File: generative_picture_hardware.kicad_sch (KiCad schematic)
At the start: 59 parts, among them J1 e_Paper_HAT, J2 Conn_ARM_JTAG_SWD_10, J3 USB_C_Receptacle_USB2.0, Q1 PMN48XP, Q2 DMG9926UDM, Q3 MBT3904DW1, SW1 SW_Push, SW2 SW_Push, U1 AP2112K-3.3, U2 ESP32-WROOM-32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

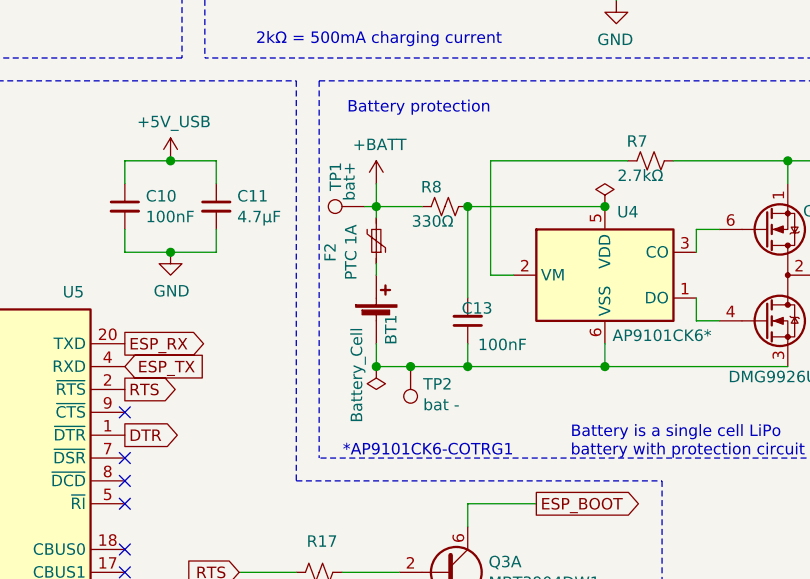
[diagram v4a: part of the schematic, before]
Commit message: Removes battery test points and adds labels to JTAG connector
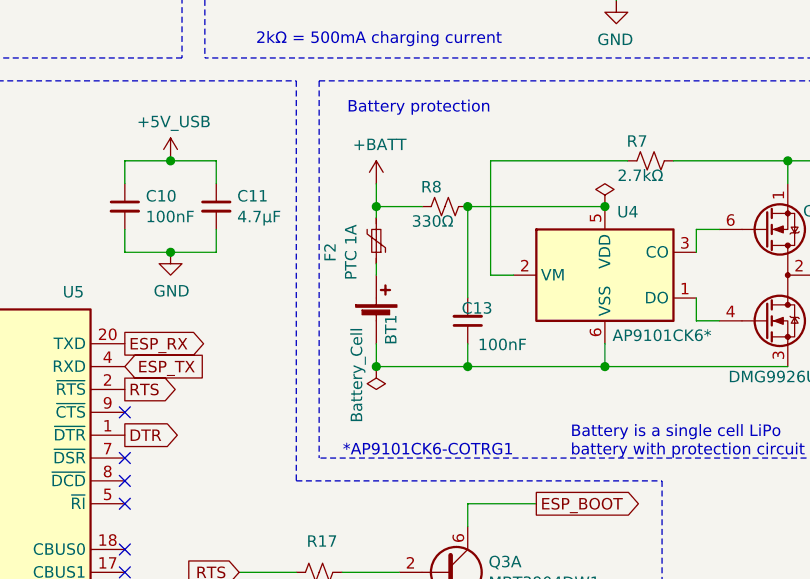
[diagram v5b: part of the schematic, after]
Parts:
- removed TP1: bat+, TestPoint:TestPoint_Pad_D2.0mm, symbol Connector:TestPoint
- removed TP2: bat -, TestPoint:TestPoint_Pad_D2.0mm, symbol Connector:TestPoint
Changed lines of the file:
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@@
   (junction (at 143.51 143.51) (diameter 1.016) (color 0 0 0 0))
   (junction (at 146.05 39.37) (diameter 1.016) (color 0 0 0 0))
-  (junction (at 147.32 143.51) (diameter 1.016) (color 0 0 0 0))
   (junction (at 153.67 125.73) (diameter 1.016) (color 0 0 0 0))
   (junction (at 153.67 143.51) (diameter 1.016) (color 0 0 0 0))
@@
     (stroke (width 0) (type solid) (color 0 0 0 0))
   )
-  (wire (pts (xy 142.24 125.73) (xy 143.51 125.73))
-    (stroke (width 0) (type solid) (color 0 0 0 0))
-  )
   (wire (pts (xy 143.51 39.37) (xy 146.05 39.37))
     (stroke (width 0) (type solid) (color 0 0 0 0))
@@
     (stroke (width 0) (type solid) (color 0 0 0 0))
   )
-  (wire (pts (xy 143.51 143.51) (xy 147.32 143.51))
+  (wire (pts (xy 143.51 143.51) (xy 153.67 143.51))
     (stroke (width 0) (type solid) (color 0 0 0 0))
   )
@@
     (stroke (width 0) (type solid) (color 0 0 0 0))
   )
-  (wire (pts (xy 147.32 143.51) (xy 153.67 143.51))
-    (stroke (width 0) (type solid) (color 0 0 0 0))
-  )
   (wire (pts (xy 153.67 125.73) (xy 153.67 135.89))
     (stroke (width 0) (type solid) (color 0 0 0 0))
@@
     (pin "1")
   )
-  (symbol (lib_id "Connector:TestPoint") (at 142.24 125.73 90) (unit 1)
-    (in_bom yes) (on_board yes)
-    (property "Reference" "TP1" (id 0) (at 139.0079 120.7771 0)
-      (effects (font (size 1.27 1.27)) (justify right))
-    )
-    (property "Value" "bat+" (id 1) (at 140.519 120.777 0)
-      (effects (font (size 1.27 1.27)) (justify right))
-    )
-    (property "Footprint" "TestPoint:TestPoint_Pad_D2.0mm" (id 2) (at 142.24 120.65 0)
-      (effects (font (size 1.27 1.27)) hide)
-    )
-    (property "Datasheet" "~" (id 3) (at 142.24 120.65 0)
-      (effects (font (size 1.27 1.27)) hide)
-    )
-    (pin "1")
-  )
-  (symbol (lib_id "Connector:TestPoint") (at 147.32 143.51 180) (unit 1)
-    (in_bom yes) (on_board yes)
-    (property "Reference" "TP2" (id 0) (at 148.7171 145.4721 0)
-      (effects (font (size 1.27 1.27)) (justify right))
-    )
-    (property "Value" "bat -" (id 1) (at 148.717 147.771 0)
-      (effects (font (size 1.27 1.27)) (justify right))
-    )
-    (property "Footprint" "TestPoint:TestPoint_Pad_D2.0mm" (id 2) (at 142.24 143.51 0)
-      (effects (font (size 1.27 1.27)) hide)
-    )
-    (property "Datasheet" "~" (id 3) (at 142.24 143.51 0)
-      (effects (font (size 1.27 1.27)) hide)
-    )
-    (pin "1")
-  )
   (symbol (lib_id "power:+3V3") (at 29.21 85.09 0) (unit 1)
     (in_bom yes) (on_board yes)
@@
       (reference "SW2") (unit 1) (value "SW_Push") (footprint "Generative_picture:SWITCH_TACTILE_CK_PTS636_SK43_SMTR_LFS")
     )
-    (path "/e9a801a9-19f2-4660-8236-021aa37015f1"
-      (reference "TP1") (unit 1) (value "bat+") (footprint "TestPoint:TestPoint_Pad_D2.0mm")
-    )
-    (path "/3610df21-61b8-4047-9c8c-5d36a128dd58"
-      (reference "TP2") (unit 1) (value "bat -") (footprint "TestPoint:TestPoint_Pad_D2.0mm")
-    )
     (path "/270f2b79-8713-40da-ba21-2980f9dd1244"

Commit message: Changes PTC footprint
It's still 1206 but with slightly wider pads.
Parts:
- F1, F2: footprint Generative_picture:Fuse_Bourns_MF-NSHT -> Generative_picture:Belfuse_0ZCJ
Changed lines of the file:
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@@
     (property "Reference" "F1" (id 0) (at 66.04 118.0908 90))
     (property "Value" "PTC 1A" (id 1) (at 66.04 120.39 90))
-    (property "Footprint" "Generative_picture:Fuse_Bourns_MF-NSHT" (id 2) (at 71.12 121.92 0)
+    (property "Footprint" "Generative_picture:Belfuse_0ZCJ" (id 2) (at 71.12 121.92 0)
       (effects (font (size 1.27 1.27)) (justify left) hide)
     )
@@
     (property "Reference" "F2" (id 0) (at 138.4108 130.81 90))
     (property "Value" "PTC 1A" (id 1) (at 140.71 130.81 90))
-    (property "Footprint" "Generative_picture:Fuse_Bourns_MF-NSHT" (id 2) (at 142.24 124.46 0)
+    (property "Footprint" "Generative_picture:Belfuse_0ZCJ" (id 2) (at 142.24 124.46 0)
       (effects (font (size 1.27 1.27)) (justify left) hide)
     )
@@
     )
     (path "/79967ec1-18c4-4b2b-9a79-8f4cedb73ca8"
-      (reference "F1") (unit 1) (value "PTC 1A") (footprint "Generative_picture:Fuse_Bourns_MF-NSHT")
+      (reference "F1") (unit 1) (value "PTC 1A") (footprint "Generative_picture:Belfuse_0ZCJ")
     )
     (path "/42dd254a-22f9-4813-9731-5f1b9e80bb9d"
-      (reference "F2") (unit 1) (value "PTC 1A") (footprint "Generative_picture:Fuse_Bourns_MF-NSHT")
+      (reference "F2") (unit 1) (value "PTC 1A") (footprint "Generative_picture:Belfuse_0ZCJ")
     )
     (path "/709e9e91-e8c6-418a-9347-6219920aa396"

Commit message: Adds Manufacturer Part Number to some components
This helps building a more useful BOM. I left out the resistors and
capacitors as the specific part is not so important.
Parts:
- D1: MPN (none) -> MBR120VLSFT3
- Q1: MPN (none) -> PMN48XP,125
- Q2: MPN (none) -> DMG9926UDM-7
- Q3: MPN (none) -> MBT3904DW1T1G
- U1: MPN (none) -> AP2112K-3.3TRG1
- U2: MPN (none) -> ESP32-WROOM-32E(M113EH2800PH3Q0)
- U3: MPN (none) -> MCP73831T-2ACI/OT
- U4: MPN (none) -> AP9101CK6-COTRG1
- U5: MPN (none) -> FT231XS-U
- U6: MPN (none) -> SRV05-4HTG-D
